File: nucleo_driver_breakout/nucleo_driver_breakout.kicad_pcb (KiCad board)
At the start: 4 copper layers, 211 x 123 mm, 108 parts, among them J1 Conn_02x18_Odd_Even, J10 Conn_01x06_Pin, J11 Conn_01x06_Pin, J12 Conn_01x04_Pin, J13 Conn_01x04_Pin, J14 Conn_01x04_Pin, J15 Conn_01x04_Pin, J2 Conn_02x18_Odd_Even, J3 ENC_1, J4 ENC_2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

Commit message: added current sense header for each motor
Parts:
- added J16: Conn_01x02_Pin, Connector_JST:JST_EH_B4B-EH-A_1x04_P2.50mm_Vertical, F.Cu at (131.0, 165.2)
- added J17: Conn_01x02_Pin, Connector_JST:JST_EH_B4B-EH-A_1x04_P2.50mm_Vertical, F.Cu at (205.4, 164.2)
- added J18: Conn_01x02_Pin, Connector_JST:JST_EH_B4B-EH-A_1x04_P2.50mm_Vertical, F.Cu at (187.3, 79.7)
- added J19: Conn_01x02_Pin, Connector_JST:JST_EH_B4B-EH-A_1x04_P2.50mm_Vertical, F.Cu at (262.4, 82.6)
- moved JP27 1.40 mm to (250.2, 76.8)
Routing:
- net M4_CS_B: track 90.8 -> 116.5 mm
- net M2_CS_B: track 137.1 -> 161.7 mm, vias 1 -> 2
- net M3_CS_B: track 63.4 -> 83.1 mm, vias 1 -> 2
- net M1_CS_B: track 126.1 -> 143.1 mm, vias 2 -> 3
- net M1_CS_A: track 132.2 -> 146.0 mm, vias 2 -> 3
- net M4_CS_A: track 92.3 -> 103.5 mm
- net M2_CS_A: track 106.5 -> 114.8 mm
- net M3_CS_A: track 72.4 -> 79.0 mm, vias 1 -> 2
- net VPDD_4: track 56.0 -> 52.1 mm
- net M4_IOUT_A: track 11.7 -> 10.4 mm
- net M4_SO-1: track 16.9 -> 15.5 mm

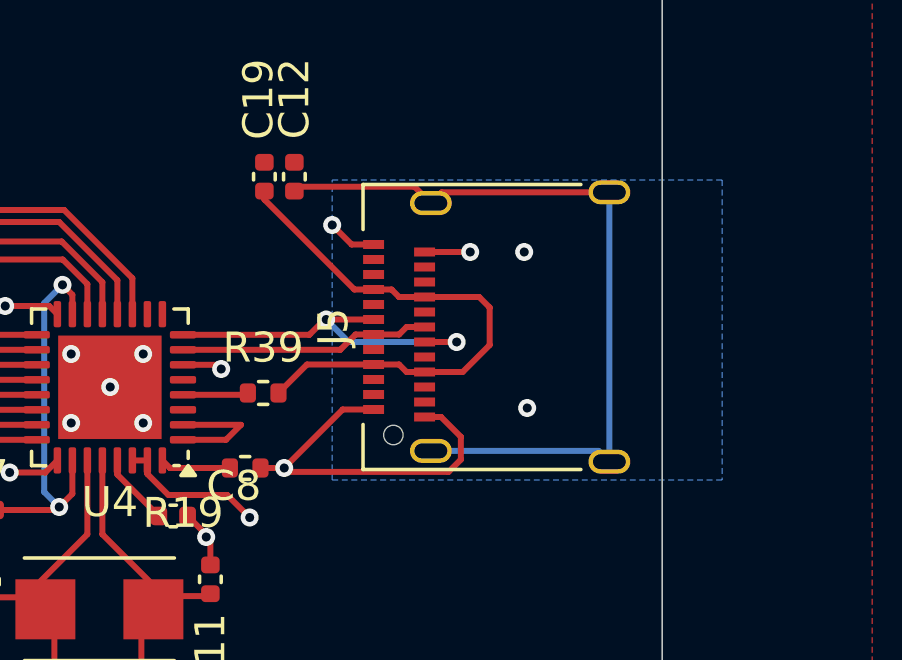
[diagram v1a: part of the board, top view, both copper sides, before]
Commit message: changed usb connector and added LCSC IDs
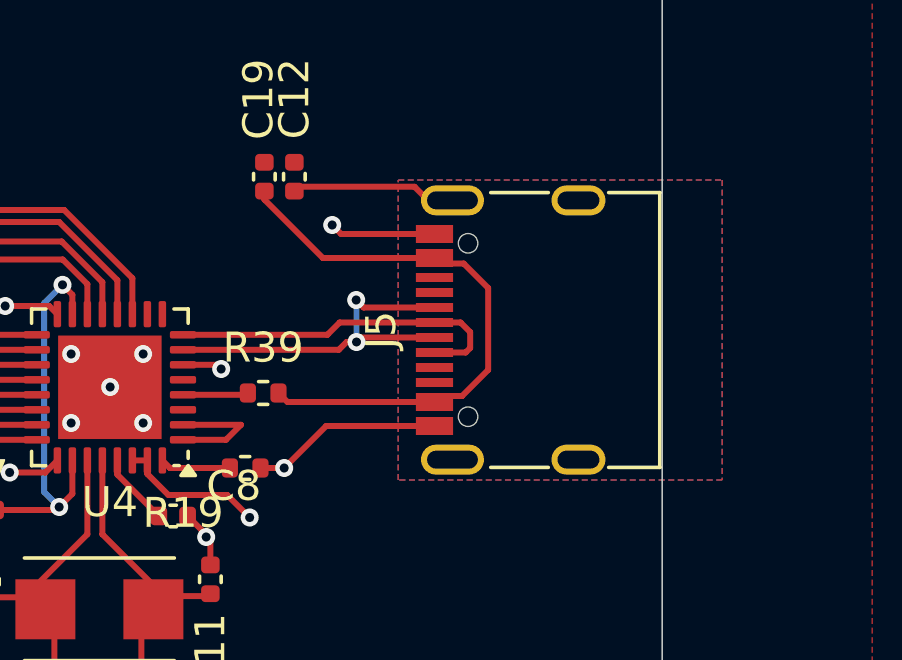
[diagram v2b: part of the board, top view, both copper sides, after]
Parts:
- J5: footprint Connector_USB:USB_C_Receptacle_Amphenol_12401610E4-2A -> Connector_USB:USB_C_Receptacle_G-Switch_GT-USB-7010ASV
- moved J5 0.74 mm to (300.1, 125.0)
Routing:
- net Net-(J5-SHIELD): track 26.0 -> 5.34 mm
- net GND: track 77.5 -> 71.4 mm, vias 86 -> 83
- net Net-(U4-DP): track 8.37 -> 12.7 mm, vias 0 -> 2
- net Net-(C19-Pad2): track 18.4 -> 19.2 mm
- net Net-(U4-DM): track 12.3 -> 11.7 mm, vias 2 -> 0
- added copper zone on F.Cu, net Net-(J5-SHIELD)

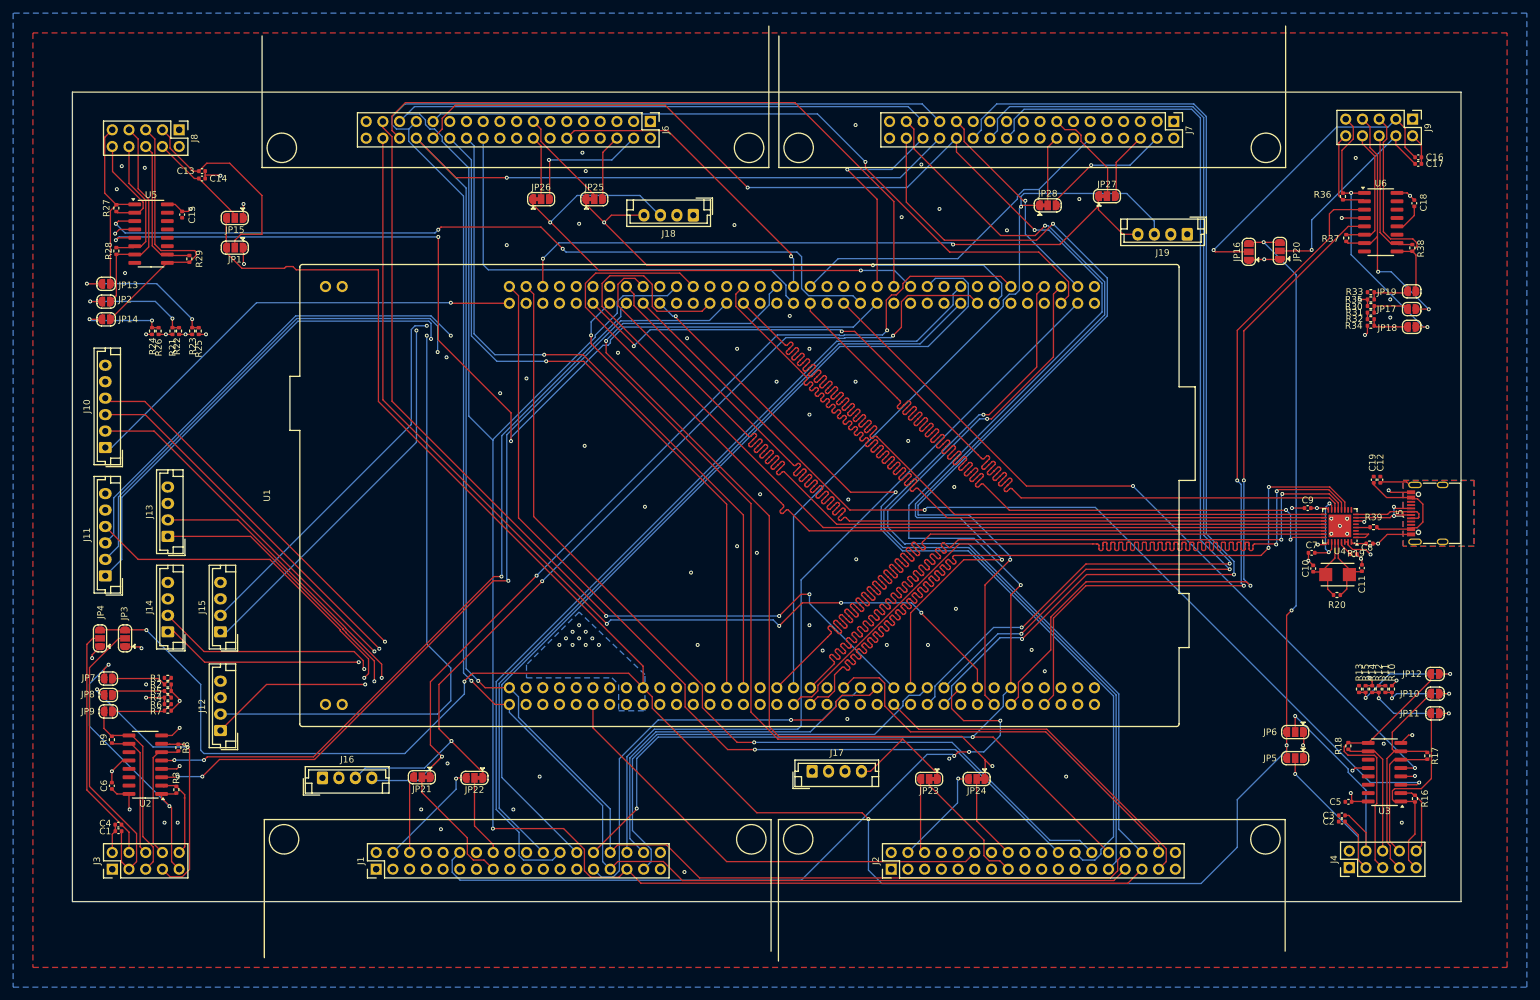
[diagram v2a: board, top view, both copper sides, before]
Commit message: added bolt holes, vias, and fixed some silkscreen overlaps
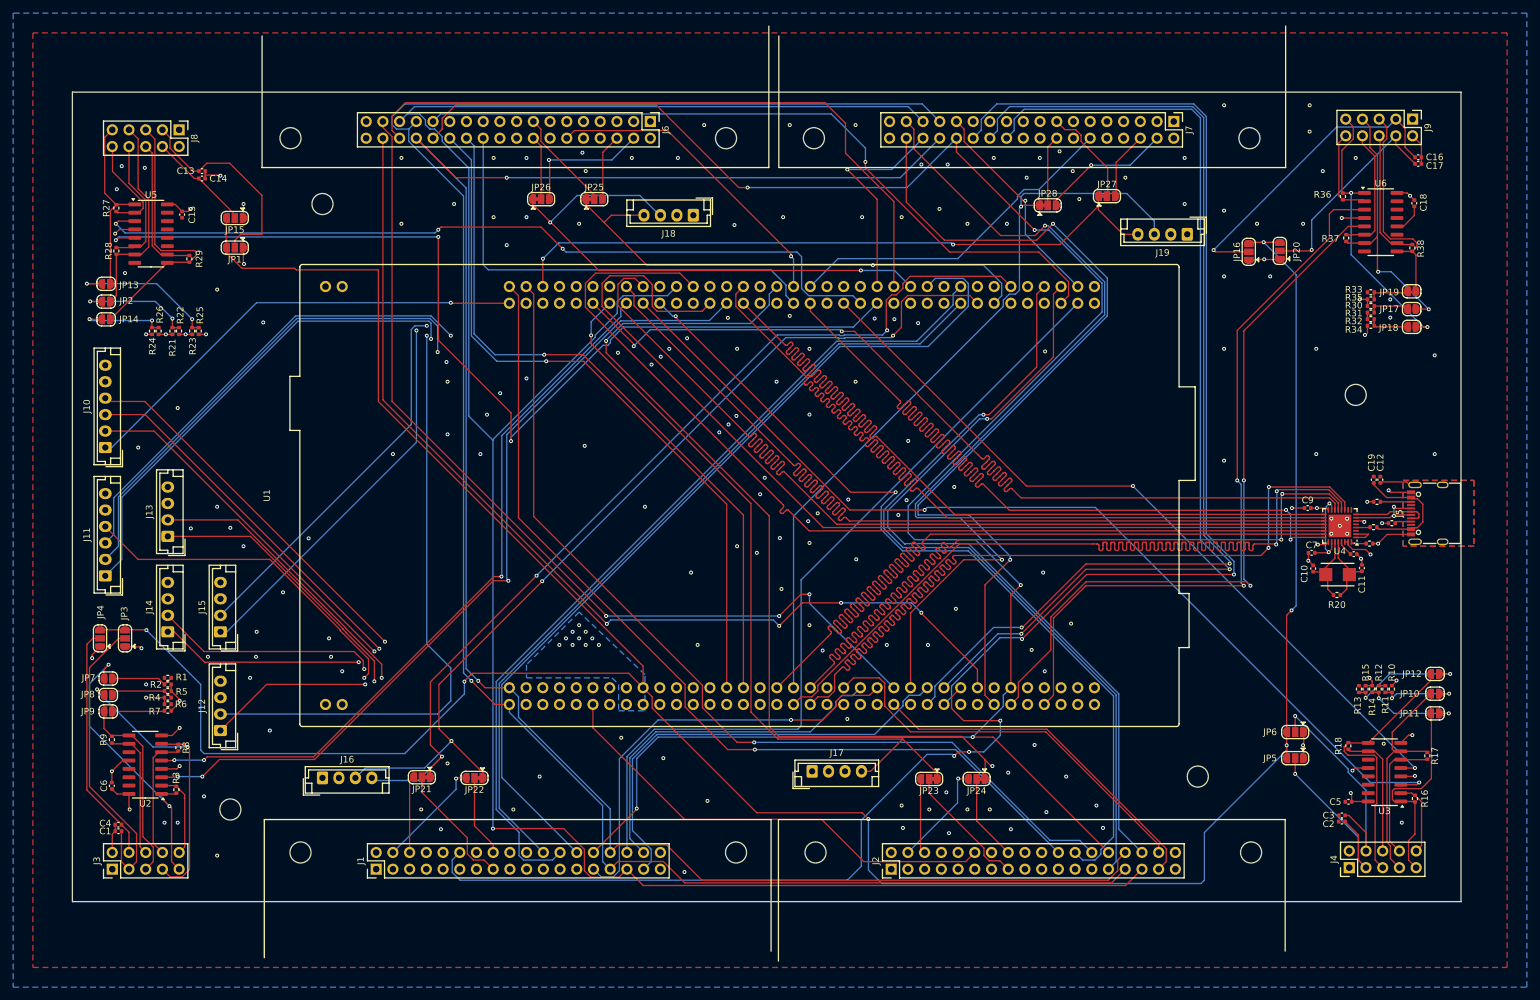
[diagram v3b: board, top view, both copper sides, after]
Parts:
- added H1: MountingHole, MountingHole:MountingHole_3.2mm_M3_ISO7380, F.Cu at (288.0, 107.0)
- added H2: MountingHole, MountingHole:MountingHole_3.2mm_M3_ISO7380, F.Cu at (131.0, 78.0)
- added H3: MountingHole, MountingHole:MountingHole_3.2mm_M3_ISO7380, F.Cu at (117.0, 170.0)
- added H4: MountingHole, MountingHole:MountingHole_3.2mm_M3_ISO7380, F.Cu at (264.0, 165.0)
- added R40: 5k1, Resistor_SMD:R_0402_1005Metric, F.Cu at (293.5, 126.5)
- added R41: 5k1, Resistor_SMD:R_0402_1005Metric, F.Cu at (291.2, 123.2)
- C19: value 3.3u -> 4.7u
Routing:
- net /USB_HS_PHY/CC2: track 0.00 -> 4.66 mm
- net VPDD_1: track 110.8 -> 114.9 mm
- net nSCS_3: track 100.1 -> 102.7 mm
- net /USB_HS_PHY/CC1: track 0.00 -> 2.51 mm
- net GND: track 71.4 -> 73.3 mm, vias 83 -> 184
- net EN-GATE_3: track 111.9 -> 113.1 mm
- net M3_CS_A: vias 2 -> 1
